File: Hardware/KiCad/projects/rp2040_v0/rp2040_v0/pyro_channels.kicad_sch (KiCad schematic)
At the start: 26 parts, among them J15 Conn_01x02, J25 Screw_Terminal_01x02, J27 Screw_Terminal_01x02, J28 Screw_Terminal_01x02, Q2 AO3400A, Q4 AO3400A, Q5 AO3400A

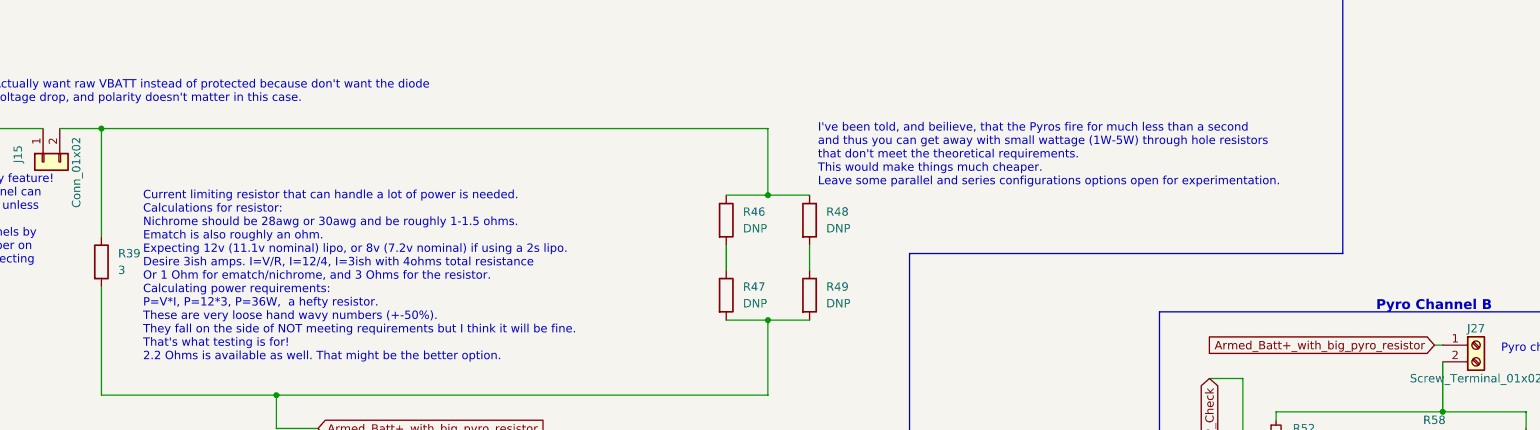
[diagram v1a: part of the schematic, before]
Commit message: Some minor changes with footprint. Sent to JLCPCB. Official Rev 0!
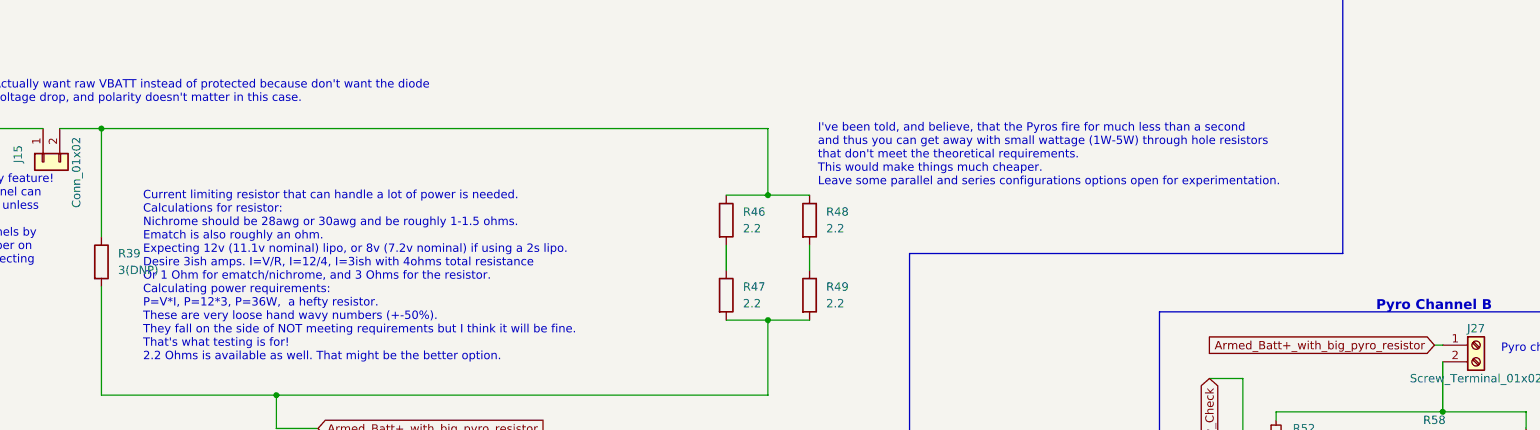
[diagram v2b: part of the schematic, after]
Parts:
- J25, J27, J28: JLC Part DNP -> Extended Part; LCSC (none) -> C557651
- Q2, Q4, Q5: LCSC (none) -> C20917
- R39: value 3 -> 3(DNP)
- R40, R42, R53, R55: footprint Resistor_SMD:R_0603_1608Metric -> Resistor_SMD:R_0402_1005Metric; LCSC (none) -> C25741
- R41, R43, R52, R54: LCSC (none) -> C23150
- R44, R56, R57: LCSC (none) -> C25744
- R45, R58, R59: LCSC (none) -> C25117
- R46, R47, R48, R49: value DNP -> 2.2; JLC Part (none) -> Basic Part; LCSC (none) -> C348866; LCSC Part (none) -> C348866
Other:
- note added: "I've been told, and believe, that the Pyros fire for much less than a second and thus you can get away with small wattage (1W-5W) through hole resistors that don't meet the theoretical requirements. This would make things much cheaper. Leave some parallel and series configurations options open for experimentation."
- note removed: "I've been told, and beilieve, that the Pyros fire for much less than a second and thus you can get away with small wattage (1W-5W) through hole resistors that don't meet the theoretical requirements. This would make things much cheaper. Leave some parallel and series configurations options open for experimentation."
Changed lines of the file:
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@@
     (effects (font (size 1.27 1.27)) (justify left bottom))
   )
-  (text "I've been told, and beilieve, that the Pyros fire for much less than a second\nand thus you can get away with small wattage (1W-5W) through hole resistors\nthat don't meet the theoretical requirements.\nThis would make things much cheaper.\nLeave some parallel and series configurations options open for experimentation."
+  (text "I've been told, and believe, that the Pyros fire for much less than a second\nand thus you can get away with small wattage (1W-5W) through hole resistors\nthat don't meet the theoretical requirements.\nThis would make things much cheaper.\nLeave some parallel and series configurations options open for experimentation."
     (at 151.13 44.45 0)
     (effects (font (size 1.27 1.27)) (justify left bottom))
@@
       (effects (font (size 1.27 1.27)) hide)
     )
+    (property "LCSC" "C20917" (id 6) (at 256.54 135.89 0)
+      (effects (font (size 1.27 1.27)) hide)
+    )
     (pin "1")
     (pin "2")
@@
       (effects (font (size 1.27 1.27)) hide)
     )
+    (property "LCSC" "C23150" (id 6) (at 59.69 123.19 0)
+      (effects (font (size 1.27 1.27)) hide)
+    )
     (pin "1")
     (pin "2")
@@
       (effects (font (size 1.27 1.27)) (justify left))
     )
-    (property "Value" "DNP" (id 1) (at 152.4 50.7999 0)
+    (property "Value" "2.2" (id 1) (at 152.4 50.7999 0)
       (effects (font (size 1.27 1.27)) (justify left))
     )
@@
     )
     (property "Datasheet" "~" (id 3) (at 149.86 49.53 0)
+      (effects (font (size 1.27 1.27)) hide)
+    )
+    (property "JLC Part" "Basic Part" (id 4) (at 149.86 49.53 0)
+      (effects (font (size 1.27 1.27)) hide)
+    )
+    (property "LCSC Part" "C348866" (id 5) (at 149.86 49.53 0)
+      (effects (font (size 1.27 1.27)) hide)
+    )
+    (property "LCSC" "C348866" (id 6) (at 149.86 49.53 0)
       (effects (font (size 1.27 1.27)) hide)
     )
@@
       (effects (font (size 1.27 1.27)) hide)
     )
-    (property "JLC Part" "DNP" (id 4) (at 251.46 68.58 0)
+    (property "JLC Part" "Extended Part" (id 4) (at 251.46 68.58 0)
       (effects (font (size 1.27 1.27)) hide)
     )
     (property "LCSC Part" "C557651" (id 5) (at 251.46 68.58 0)
+      (effects (font (size 1.27 1.27)) hide)
+    )
+    (property "LCSC" "C557651" (id 6) (at 251.46 68.58 0)
       (effects (font (size 1.27 1.27)) hide)
     )
@@
       (effects (font (size 1.27 1.27)) (justify left))
     )
-    (property "Value" "DNP" (id 1) (at 152.4 62.2299 0)
+    (property "Value" "2.2" (id 1) (at 152.4 62.2299 0)
       (effects (font (size 1.27 1.27)) (justify left))
     )
@@
       (effects (font (size 1.27 1.27)) hide)
     )
+    (property "JLC Part" "Basic Part" (id 4) (at 149.86 60.96 0)
+      (effects (font (size 1.27 1.27)) hide)
+    )
+    (property "LCSC Part" "C348866" (id 5) (at 149.86 60.96 0)
+      (effects (font (size 1.27 1.27)) hide)
+    )
+    (property "LCSC" "C348866" (id 6) (at 149.86 60.96 0)
+      (effects (font (size 1.27 1.27)) hide)
+    )
     (pin "1")
     (pin "2")
@@
       (effects (font (size 1.27 1.27)) (justify left))
     )
-    (property "Value" "DNP" (id 1) (at 139.7 62.2299 0)
+    (property "Value" "2.2" (id 1) (at 139.7 62.2299 0)
       (effects (font (size 1.27 1.27)) (justify left))
     )
@@
       (effects (font (size 1.27 1.27)) hide)
     )
+    (property "JLC Part" "Basic Part" (id 4) (at 137.16 60.96 0)
+      (effects (font (size 1.27 1.27)) hide)
+    )
+    (property "LCSC Part" "C348866" (id 5) (at 137.16 60.96 0)
+      (effects (font (size 1.27 1.27)) hide)
+    )
+    (property "LCSC" "C348866" (id 6) (at 137.16 60.96 0)
+      (effects (font (size 1.27 1.27)) hide)
+    )
     (pin "1")
     (pin "2")
@@
     )
     (property "JLC Part" "Basic Part" (id 5) (at 64.77 173.99 0)
+      (effects (font (size 1.27 1.27)) hide)
+    )
+    (property "LCSC" "C23150" (id 6) (at 64.77 173.99 0)
       (effects (font (size 1.27 1.27)) hide)
     )
@@
     )
     (property "JLC Part" "Basic Part" (id 5) (at 220.98 82.55 0)
+      (effects (font (size 1.27 1.27)) hide)
+    )
+    (property "LCSC" "C23150" (id 6) (at 220.98 82.55 0)
       (effects (font (size 1.27 1.27)) hide)
     )
@@
       (effects (font (size 1.27 1.27)) hide)
     )
-    (property "JLC Part" "DNP" (id 4) (at 90.17 105.41 0)
+    (property "JLC Part" "Extended Part" (id 4) (at 90.17 105.41 0)
       (effects (font (size 1.27 1.27)) hide)
     )
     (property "LCSC Part" "C557651" (id 5) (at 90.17 105.41 0)
+      (effects (font (size 1.27 1.27)) hide)
+    )
+    (property "LCSC" "C557651" (id 6) (at 90.17 105.41 0)
       (effects (font (size 1.27 1.27)) hide)
     )
@@
       (effects (font (size 1.27 1.27)) hide)
     )
+    (property "LCSC" "C25117" (id 6) (at 245.11 86.36 0)
+      (effects (font (size 1.27 1.27)) hide)
+    )
     (pin "1")
     (pin "2")
@@
       (effects (font (size 1.27 1.27)) hide)
     )
+    (property "LCSC" "C23150" (id 6) (at 220.98 132.08 0)
+      (effects (font (size 1.27 1.27)) hide)
+    )
     (pin "1")
     (pin "2")
@@
       (effects (font (size 1.27 1.27)) (justify left))
     )
-    (property "Footprint" "Resistor_SMD:R_0603_1608Metric" (id 2) (at 220.98 92.71 0)
+    (property "Footprint" "Resistor_SMD:R_0402_1005Metric" (id 2) (at 220.98 92.71 0)
       (effects (font (size 1.27 1.27)) hide)
     )
@@
     )
     (property "JLC Part" "Basic Part" (id 5) (at 220.98 92.71 0)
+      (effects (font (size 1.27 1.27)) hide)
+    )
+    (property "LCSC" "C25741" (id 6) (at 220.98 92.71 0)
       (effects (font (size 1.27 1.27)) hide)
     )
@@
       (effects (font (size 1.27 1.27)) hide)
     )
+    (property "LCSC" "C25117" (id 6) (at 104.14 133.35 0)
+      (effects (font (size 1.27 1.27)) hide)
+    )
     (pin "1")
     (pin "2")
@@
       (effects (font (size 1.27 1.27)) hide)
     )
+    (property "LCSC" "C25744" (id 6) (at 97.79 138.43 0)
+      (effects (font (size 1.27 1.27)) hide)
+    )
     (pin "1")
     (pin "2")
@@
       (effects (font (size 1.27 1.27)) hide)
     )
+    (property "LCSC" "C20917" (id 6) (at 256.54 86.36 0)
+      (effects (font (size 1.27 1.27)) hide)
+    )
     (pin "1")
     (pin "2")
@@
       (effects (font (size 1.27 1.27)) (justify left))
     )
-    (property "Footprint" "Resistor_SMD:R_0603_1608Metric" (id 2) (at 55.88 186.69 0)
+    (property "Footprint" "Resistor_SMD:R_0402_1005Metric" (id 2) (at 55.88 186.69 0)
       (effects (font (size 1.27 1.27)) hide)
     )
@@
     )
     (property "JLC Part" "Basic Part" (id 5) (at 55.88 186.69 0)
+      (effects (font (size 1.27 1.27)) hide)
+    )
+    (property "LCSC" "C25741" (id 6) (at 55.88 186.69 0)
       (effects (font (size 1.27 1.27)) hide)
     )
@@
       (effects (font (size 1.27 1.27)) hide)
     )
+    (property "LCSC" "C25744" (id 6) (at 238.76 140.97 0)
+      (effects (font (size 1.27 1.27)) hide)
+    )
     (pin "1")
     (pin "2")
@@
       (effects (font (size 1.27 1.27)) (justify left))
     )
-    (property "Footprint" "Resistor_SMD:R_0603_1608Metric" (id 2) (at 59.69 138.43 0)
+    (property "Footprint" "Resistor_SMD:R_0402_1005Metric" (id 2) (at 59.69 138.43 0)
       (effects (font (size 1.27 1.27)) hide)
     )
@@
     )
     (property "JLC Part" "Basic Part" (id 5) (at 59.69 138.43 0)
+      (effects (font (size 1.27 1.27)) hide)
+    )
+    (property "LCSC" "C25741" (id 6) (at 59.69 138.43 0)
       (effects (font (size 1.27 1.27)) hide)
     )
@@
       (effects (font (size 1.27 1.27)) hide)
     )
+    (property "LCSC" "C25744" (id 6) (at 238.76 91.44 0)
+      (effects (font (size 1.27 1.27)) hide)
+    )
     (pin "1")
     (pin "2")
@@
       (effects (font (size 1.27 1.27)) (justify left))
     )
-    (property "Value" "DNP" (id 1) (at 139.7 50.7999 0)
+    (property "Value" "2.2" (id 1) (at 139.7 50.7999 0)
       (effects (font (size 1.27 1.27)) (justify left))
     )
@@
     )
     (property "Datasheet" "~" (id 3) (at 137.16 49.53 0)
+      (effects (font (size 1.27 1.27)) hide)
+    )
+    (property "JLC Part" "Basic Part" (id 4) (at 137.16 49.53 0)
+      (effects (font (size 1.27 1.27)) hide)
+    )
+    (property "LCSC Part" "C348866" (id 5) (at 137.16 49.53 0)
+      (effects (font (size 1.27 1.27)) hide)
+    )
+    (property "LCSC" "C348866" (id 6) (at 137.16 49.53 0)
       (effects (font (size 1.27 1.27)) hide)
     )
@@
       (effects (font (size 1.27 1.27)) hide)
     )
-    (property "JLC Part" "DNP" (id 4) (at 251.46 118.11 0)
+    (property "JLC Part" "Extended Part" (id 4) (at 251.46 118.11 0)
       (effects (font (size 1.27 1.27)) hide)
     )
     (property "LCSC Part" "C557651" (id 5) (at 251.46 118.11 0)
+      (effects (font (size 1.27 1.27)) hide)
+    )
+    (property "LCSC" "C557651" (id 6) (at 251.46 118.11 0)
       (effects (font (size 1.27 1.27)) hide)
     )
@@
       (effects (font (size 1.27 1.27)) hide)
     )
+    (property "LCSC" "C25117" (id 6) (at 245.11 135.89 0)
+      (effects (font (size 1.27 1.27)) hide)
+    )
     (pin "1")
     (pin "2")
@@
       (effects (font (size 1.27 1.27)) (justify left))
     )
-    (property "Footprint" "Resistor_SMD:R_0603_1608Metric" (id 2) (at 220.98 142.24 0)
+    (property "Footprint" "Resistor_SMD:R_0402_1005Metric" (id 2) (at 220.98 142.24 0)
       (effects (font (size 1.27 1.27)) hide)
     )
@@
       (effects (font (size 1.27 1.27)) hide)
     )
+    (property "LCSC" "C25741" (id 6) (at 220.98 142.24 0)
+      (effects (font (size 1.27 1.27)) hide)
+    )
     (pin "1")
     (pin "2")
@@
       (effects (font (size 1.27 1.27)) (justify left))
     )
-    (property "Value" "3" (id 1) (at 44.45 57.1499 0)
+    (property "Value" "3(DNP)" (id 1) (at 44.45 57.1499 0)
       (effects (font (size 1.27 1.27)) (justify left))
     )
@@
       (effects (font (size 1.27 1.27)) hide)
     )
+    (property "LCSC" "C20917" (id 6) (at 115.57 133.35 0)
+      (effects (font (size 1.27 1.27)) hide)
+    )
